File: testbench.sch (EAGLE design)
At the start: 97 parts, among them IC1 74LS595D, IC2 74LS595D, Q1 MOSFET-N, Q2 MOSFET-N, Q3 MOSFET-N, Q4 MOSFET-N, Q5 MOSFET-N, Q6 MOSFET-N, U1 ATMEGA328P_TQFP, U2 KA7805ERTF, Y1 20MHz

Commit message: v 1.0 - REV_A
You can find all the gerbers and the BOM. Sent to Fab House.
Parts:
- added F1: PTCSMD-W, SparkFun-PowerIC:PTCSMD-W
- +24V, +5V, LED1, LED10, LED11, LED12, LED13, LED14, LED15, LED16, LED17, LED18, LED2, LED3, LED4, LED5, LED6, LED7, LED8, LED9: MF (none) -> MULTICOMP; MPN (none) -> OVS-0803; OC_FARNELL (none) -> 1716765
- C1, C10, C11, C12, C13, C15, C16, C17, C18, C19, C2, C3, C4, C5, C6, C9: MF (none) -> AVX; MPN (none) -> 08051C104KAT2A; OC_FARNELL (none) -> 1740681
- C14: MF (none) -> AVX; MPN (none) -> 08055C334KAT2A; OC_FARNELL (none) -> 1657934
- C7, C8: MF (none) -> AVX; MPN (none) -> 08051A220JAT2A; OC_FARNELL (none) -> 317500
- D1, D2, D3, D4, D5, D6, D7: MF (none) -> DIODES INC.; MPN (none) -> B140-13-F; OC_FARNELL (none) -> 1843670
- HOTEND1, HOTEND2, HOTEND3, HOTEND4, HOTEND5, HOTEND6, ICSP, JP8: OC_FARNELL (none) -> unknown
- IC1, IC2: MF (none) -> TEXAS INSTRUMENTS; MPN (none) -> SN74AHCT595D; OC_FARNELL (none) -> 1740114
- PC1: MF (none) -> MOLEX; MPN (none) -> 39303045; OC_FARNELL (none) -> 9963553
- Q1, Q2, Q3, Q4, Q5, Q6: MF (none) -> INTERNATIONAL RECTIFIER; MPN (none) -> IRF8736PBF; OC_FARNELL (none) -> 1551903
- R1, R13, R17, R21, R25, R5, R9: MF (none) -> MULTICOMP; MPN (none) -> MCWR08X5601FTL; OC_FARNELL (none) -> 2447693
- R10, R14, R18, R2, R22, R6: MF (none) -> PANASONIC ELECTRONIC COMPONENTS; MPN (none) -> ERA6AEB101V; OC_FARNELL (none) -> 1577644
- R11, R15, R19, R23, R26, R3, R7: MF (none) -> BOURNS; MPN (none) -> 0621-013K500-AB103; OC_FARNELL (none) -> 2469474
- R12, R16, R20, R24, R4, R8: MF (none) -> TE CONNECTIVITY; MPN (none) -> 1-2176085-7; OC_FARNELL (none) -> 2118118
- R27: MF (none) -> BOURNS; MPN (none) -> CR0805-JW-102ELF; OC_FARNELL (none) -> 2008389
- RESET: MF (none) -> PANASONIC ELECTRONIC COMPONENTS; MPN (none) -> EVQQ2503W; OC_FARNELL (none) -> 9962913
- U1: MF (none) -> ATMEL; MPN (none) -> ATMEGA328-AU; OC_FARNELL (none) -> 1972086
- U2: MF (none) -> FAIRCHILD SEMICONDUCTOR; MPN (none) -> KA7805ERTF; OC_FARNELL (none) -> 2102585
- Y1: MF (none) -> TXC; MPN (none) -> 9B-20.000MAAJ-B; OC_FARNELL (none) -> 1842224
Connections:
- new net +24VHE: D1.C, D2.C, D3.C, D4.C, D5.C, D6.C, F1.2, HOTEND1.1, HOTEND2.1, HOTEND3.1, HOTEND4.1, HOTEND5.1, HOTEND6.1, R1.2, R13.2, R17.2, R21.2, R5.2, R9.2
- net +24V: now also F1.1; no longer D1.C, D2.C, D3.C, D4.C, D5.C, D6.C, HOTEND1.1, HOTEND2.1, HOTEND3.1, HOTEND4.1, HOTEND5.1, HOTEND6.1, R1.2, R13.2, R17.2, R21.2, R5.2, R9.2
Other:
- note added: "A"
- note added: "version 1.0"
- moved on the sheet: +24V, +5V, C1, C10, C11, C12, C13, C14, C15, C16, C17, C18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

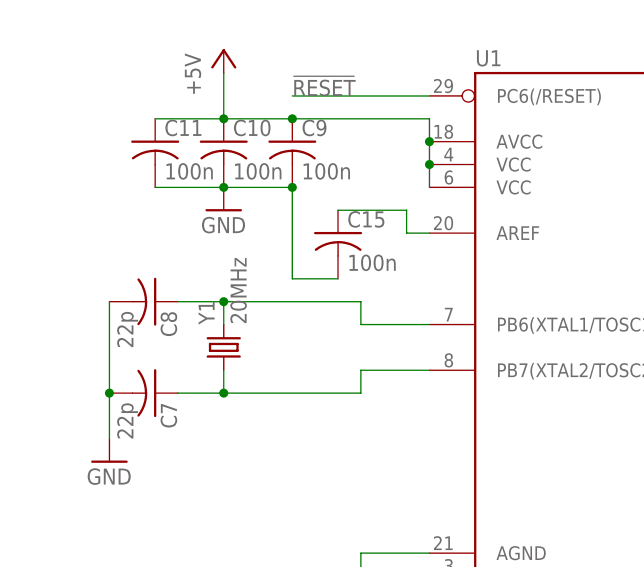
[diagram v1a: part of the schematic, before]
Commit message: All the code for the Hotend Test Jig!
Updated BOM
All the code, untested yet
Updated crystal frequency
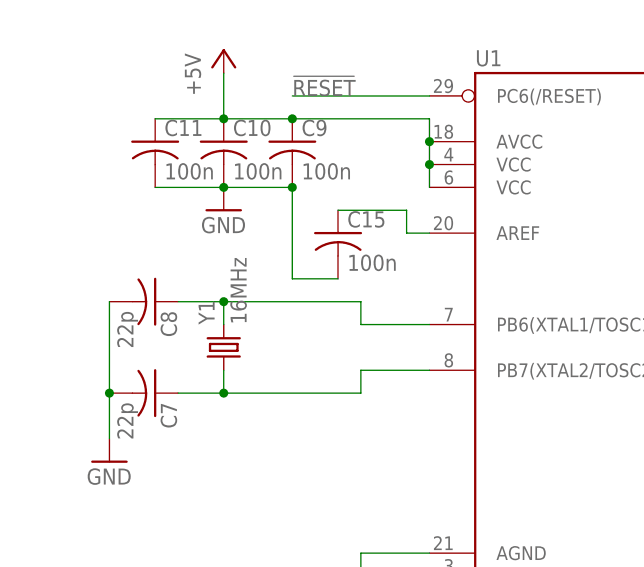
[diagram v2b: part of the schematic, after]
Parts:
- Y1: value 20MHz -> 16MHz
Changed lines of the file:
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@@
 <attribute name="OC_FARNELL" value="1972086"/>
 </part>
-<part name="Y1" library="SparkFun-FreqCtrl" deviceset="CRYSTAL" device="HC49US" value="20MHz">
+<part name="Y1" library="SparkFun-FreqCtrl" deviceset="CRYSTAL" device="HC49US" value="16MHz">
 <attribute name="MF" value="TXC"/>
 <attribute name="MPN" value="9B-20.000MAAJ-B"/>
